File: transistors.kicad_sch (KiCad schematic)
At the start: 16 parts, among them J11 Transistor_2, J12 Transistor_1, J13 Transistor_4, J14 Transistor_.3, Q1 DMN2011UTS, Q2 DMN2011UTS, Q3 DMN2011UTS, Q4 DMN2011UTS

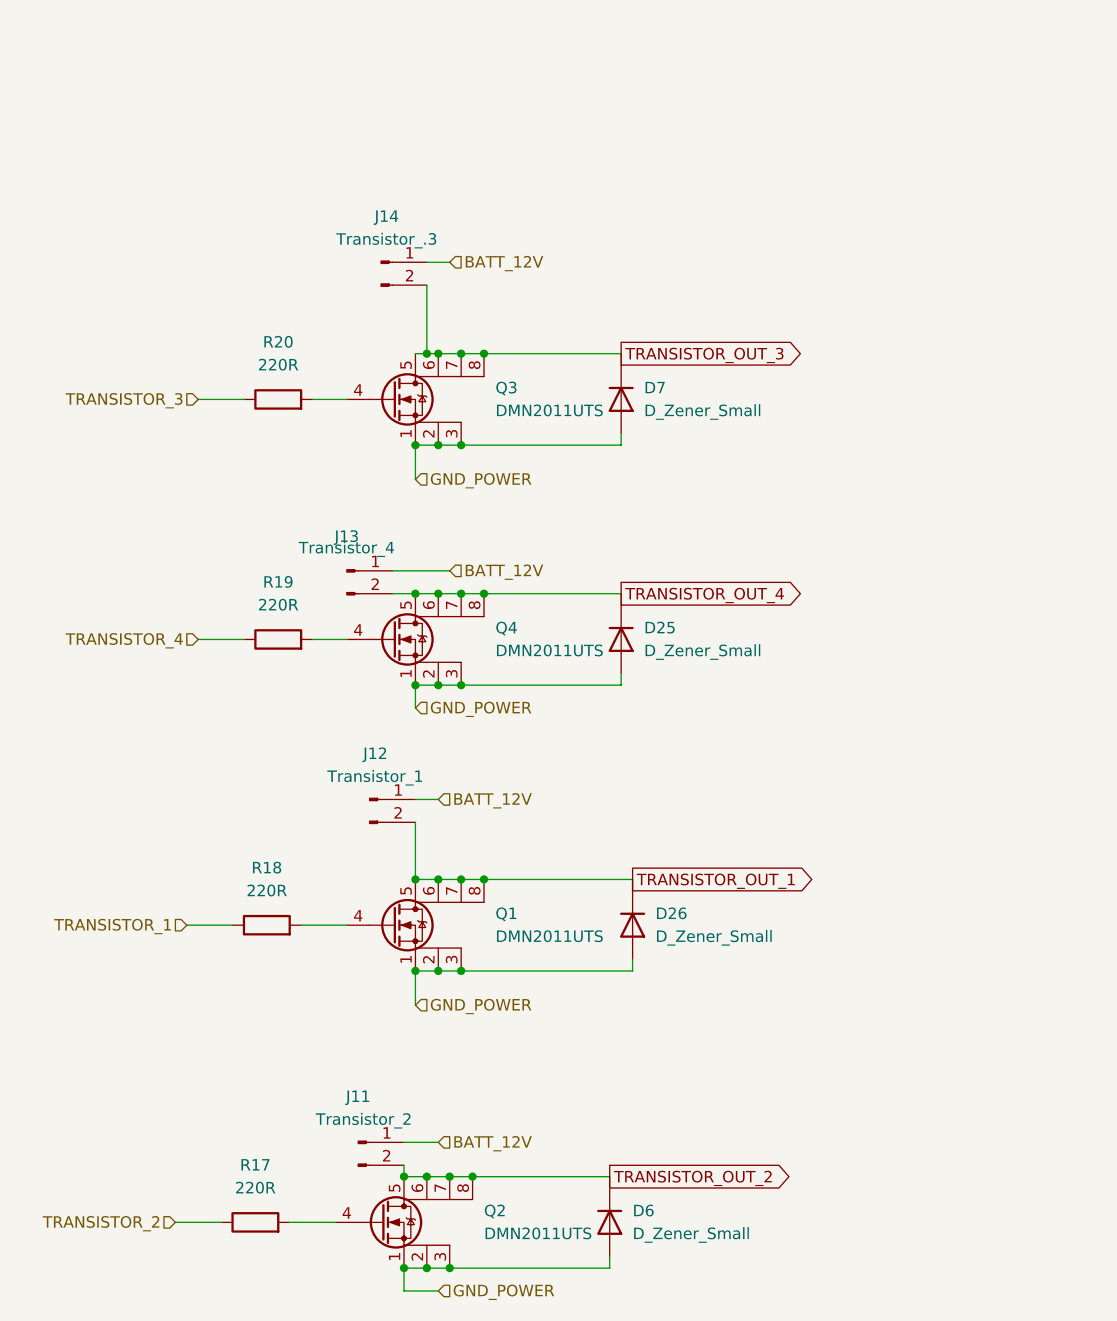
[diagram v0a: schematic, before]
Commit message: add possibility to have 2 of the transistor outputs to use either 12V or 24V
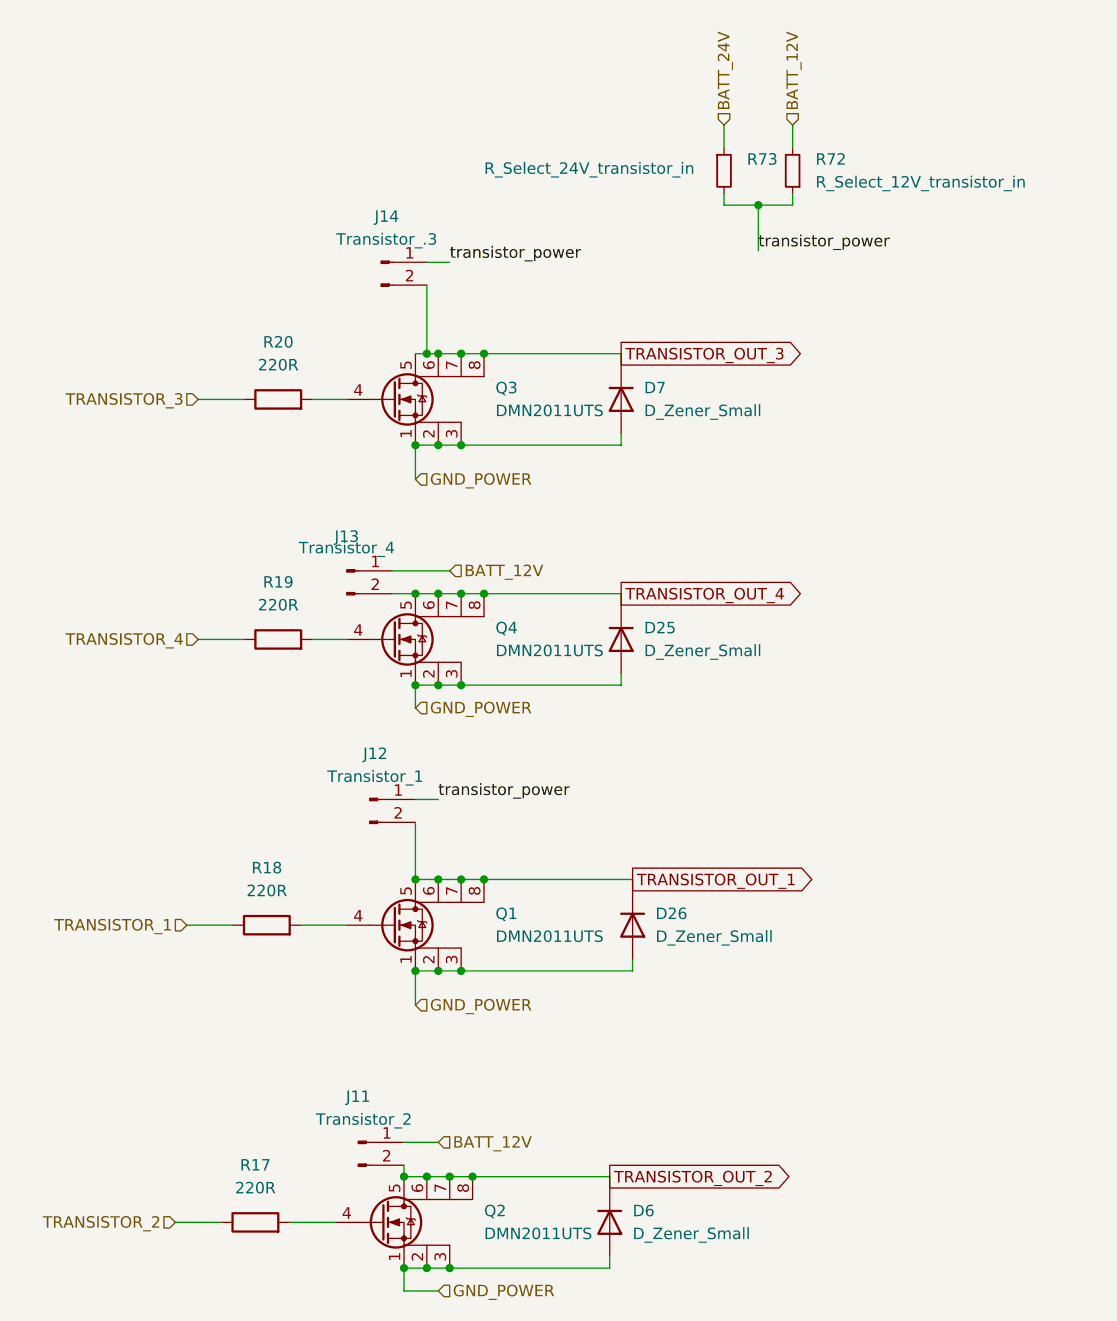
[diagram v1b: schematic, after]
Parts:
- added R72: R_Select_12V_transistor_in, Resistor_SMD:R_1206_3216Metric, symbol Device:R_Small
- added R73: R_Select_24V_transistor_in, Resistor_SMD:R_1206_3216Metric, symbol Device:R_Small
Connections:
- net BATT_12V: now also R72.2; no longer J12.1 (Pin_1), J14.1 (Pin_1)
- new net BATT_24V: R73.1
- new net transistor_power: J12.1 (Pin_1), J14.1 (Pin_1), R72.1, R73.2
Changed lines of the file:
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@@
+	)
+	(junction
+		(at 227.33 34.29)
+		(diameter 0)
+		(color 0 0 0 0)
 	)
 	(junction
@@
 	(wire
 		(pts
+			(xy 223.52 33.02) (xy 223.52 34.29)
+		)
+		(stroke
+			(width 0)
+			(type default)
+		)
+	)
+	(wire
+		(pts
 			(xy 189.23 87.63) (xy 191.77 87.63)
 		)
@@
 	(wire
 		(pts
+			(xy 231.14 34.29) (xy 231.14 33.02)
+		)
+		(stroke
+			(width 0)
+			(type default)
+		)
+	)
+	(wire
+		(pts
 			(xy 190.5 50.8) (xy 191.77 50.8)
 		)
@@
 	(wire
 		(pts
+			(xy 231.14 25.4) (xy 231.14 27.94)
+		)
+		(stroke
+			(width 0)
+			(type default)
+		)
+	)
+	(wire
+		(pts
 			(xy 189.23 60.96) (xy 191.77 60.96)
 		)
@@
 	(wire
 		(pts
+			(xy 223.52 34.29) (xy 227.33 34.29)
+		)
+		(stroke
+			(width 0)
+			(type default)
+		)
+	)
+	(wire
+		(pts
 			(xy 194.31 60.96) (xy 212.09 60.96)
 		)
@@
 	(wire
 		(pts
+			(xy 223.52 25.4) (xy 223.52 27.94)
+		)
+		(stroke
+			(width 0)
+			(type default)
+		)
+	)
+	(wire
+		(pts
 			(xy 189.23 60.96) (xy 189.23 64.77)
 		)
@@
 	(wire
 		(pts
+			(xy 231.14 34.29) (xy 227.33 34.29)
+		)
+		(stroke
+			(width 0)
+			(type default)
+		)
+	)
+	(wire
+		(pts
+			(xy 227.33 34.29) (xy 227.33 39.37)
+		)
+		(stroke
+			(width 0)
+			(type default)
+		)
+	)
+	(wire
+		(pts
 			(xy 187.96 154.94) (xy 187.96 152.4)
 		)
@@
 			(width 0)
 			(type default)
+		)
+	)
+	(label "transistor_power"
+		(at 191.77 100.33 0)
+		(effects
+			(font
+				(size 1.27 1.27)
+			)
+			(justify left bottom)
+		)
+	)
+	(label "transistor_power"
+		(at 193.04 40.64 0)
+		(effects
+			(font
+				(size 1.27 1.27)
+			)
+			(justify left bottom)
+		)
+	)
+	(label "transistor_power"
+		(at 227.33 39.37 0)
+		(effects
+			(font
+				(size 1.27 1.27)
+			)
+			(justify left bottom)
 		)
 	)
@@
 		)
 	)
-	(hierarchical_label "BATT_12V"
-		(shape input)
-		(at 193.04 40.64 0)
-		(effects
-			(font
-				(size 1.27 1.27)
-			)
-			(justify left)
-		)
-	)
 	(hierarchical_label "GND_POWER"
 		(shape input)
@@
 		)
 	)
+	(hierarchical_label "BATT_12V"
+		(shape input)
+		(at 193.04 74.93 0)
+		(effects
+			(font
+				(size 1.27 1.27)
+			)
+			(justify left)
+		)
+	)
 	(hierarchical_label "GND_POWER"
 		(shape input)
@@
 		)
 	)
-	(hierarchical_label "BATT_12V"
-		(shape input)
-		(at 191.77 100.33 0)
-		(effects
-			(font
-				(size 1.27 1.27)
-			)
-			(justify left)
-		)
-	)
 	(hierarchical_label "TRANSISTOR_1"
 		(shape input)
@@
 		)
 	)
+	(hierarchical_label "BATT_24V"
+		(shape input)
+		(at 223.52 25.4 90)
+		(effects
+			(font
+				(size 1.27 1.27)
+			)
+			(justify left)
+		)
+	)
 	(hierarchical_label "BATT_12V"
 		(shape input)
-		(at 193.04 74.93 0)
+		(at 231.14 25.4 90)
 		(effects
 			(font
@@
 	)
 	(symbol
+		(lib_id "Device:R_Small")
+		(at 223.52 30.48 0)
+		(unit 1)
+		(exclude_from_sim no)
+		(in_bom yes)
+		(on_board yes)
+		(dnp no)
+		(property "Reference" "R73"
+			(at 226.06 29.2099 0)
+			(effects
+				(font
+					(size 1.27 1.27)
+				)
+				(justify left)
+			)
+		)
+		(property "Value" "R_Select_24V_transistor_in"
+			(at 196.85 30.226 0)
+			(effects
+				(font
+					(size 1.27 1.27)
+				)
+				(justify left)
+			)
+		)
+		(property "Footprint" "Resistor_SMD:R_1206_3216Metric"
+			(at 223.52 30.48 0)
+			(effects
+				(font
+					(size 1.27 1.27)
+				)
+				(hide yes)
+			)
+		)
+		(property "Datasheet" "~"
+			(at 223.52 30.48 0)
+			(effects
+				(font
+					(size 1.27 1.27)
+				)
+				(hide yes)
+			)
+		)
+		(property "Description" "Resistor, small symbol"
+			(at 223.52 30.48 0)
+			(effects
+				(font
+					(size 1.27 1.27)
+				)
+				(hide yes)
+			)
+		)
+		(pin "2"
+		)
+		(pin "1"
+		)
+		(instances
+			(project "carte_servo"
+				(path "/e63e39d7-6ac0-4ffd-8aa3-1841a4541b55/8cf8b4bb-2251-4ebd-baba-4f57c988e66e"
+					(reference "R73")
+					(unit 1)
+				)
+			)
+		)
+	)
+	(symbol
 		(lib_id "Device:D")
 		(at 212.09 55.88 270)
@@
 					(unit 1)
 				)
+			)
+		)
+	)
+	(symbol
+		(lib_id "Device:R_Small")
+		(at 231.14 30.48 180)
+		(unit 1)
+		(exclude_from_sim no)
+		(in_bom yes)
+		(on_board yes)
+		(dnp no)
+		(fields_autoplaced yes)
+		(property "Reference" "R72"
+			(at 233.68 29.2099 0)
+			(effects
+				(font
+					(size 1.27 1.27)
+				)
+				(justify right)
+			)
+		)
+		(property "Value" "R_Select_12V_transistor_in"
+			(at 233.68 31.7499 0)
+			(effects
+				(font
+					(size 1.27 1.27)
+				)
+				(justify right)
+			)
+		)
+		(property "Footprint" "Resistor_SMD:R_1206_3216Metric"
+			(at 231.14 30.48 0)
+			(effects
+				(font
+					(size 1.27 1.27)
+				)
+				(hide yes)
+			)
+		)
+		(property "Datasheet" "~"
+			(at 231.14 30.48 0)
+			(effects
+				(font
+					(size 1.27 1.27)
+				)
+				(hide yes)
+			)
+		)
+		(property "Description" "Resistor, small symbol"
+			(at 231.14 30.48 0)
+			(effects
+				(font
+					(size 1.27 1.27)
+				)
+				(hide yes)
+			)
+		)
+		(pin "2"
+		)
+		(pin "1"
+		)
+		(instances
+			(project "carte_servo"
+				(path "/e63e39d7-6ac0-4ffd-8aa3-1841a4541b55/8cf8b4bb-2251-4ebd-baba-4f57c988e66e"
+					(reference "R72")
+					(unit 1)
+				)

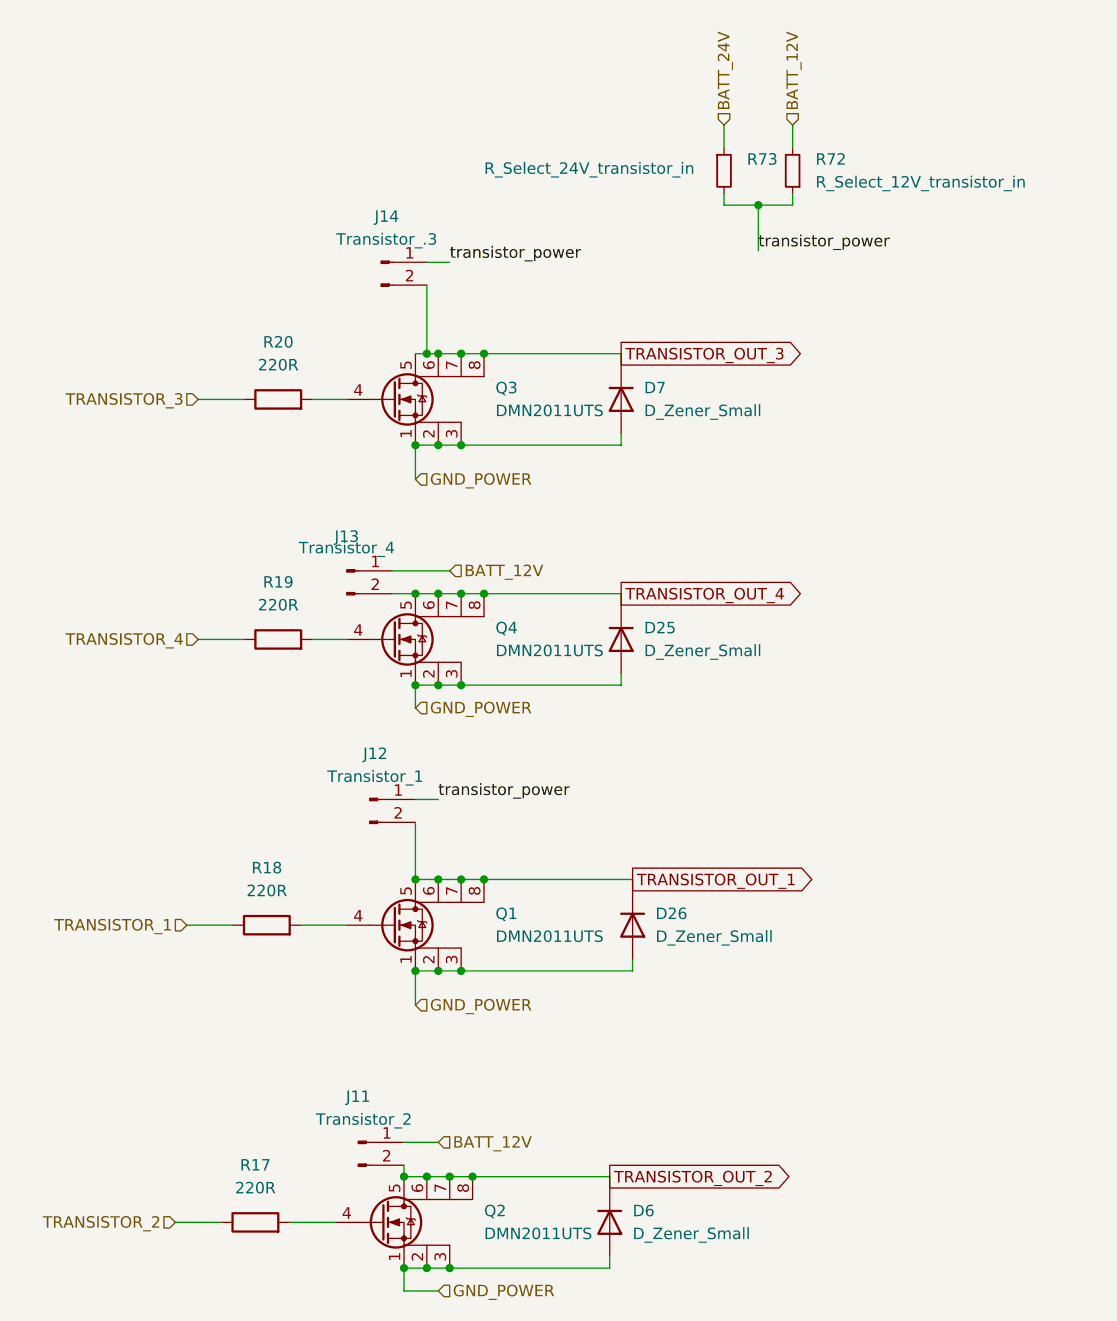
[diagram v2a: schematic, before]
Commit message: fix warnings + add big capa on 6V DCDC input
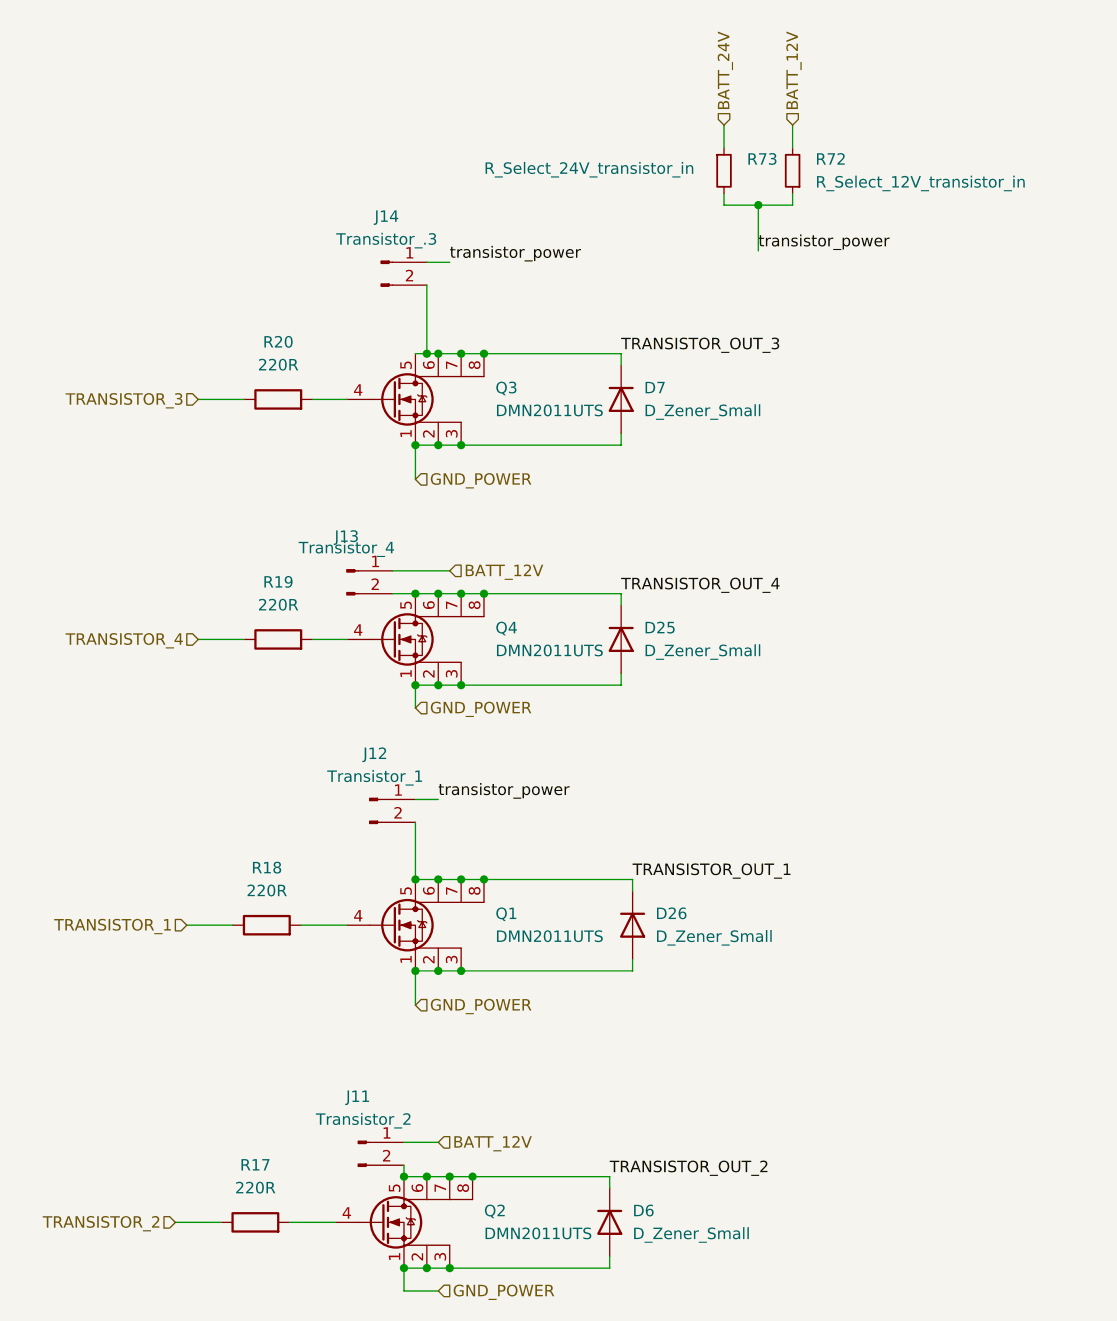
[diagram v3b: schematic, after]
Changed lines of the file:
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@@
+		)
+	)
+	(label "TRANSISTOR_OUT_3"
+		(at 212.09 50.8 0)
+		(effects
+			(font
+				(size 1.27 1.27)
+			)
+			(justify left bottom)
+		)
+	)
+	(label "TRANSISTOR_OUT_4"
+		(at 212.09 77.47 0)
+		(effects
+			(font
+				(size 1.27 1.27)
+			)
+			(justify left bottom)
 		)
 	)
@@
 		)
 	)
-	(global_label "TRANSISTOR_OUT_1"
-		(shape output)
-		(at 213.36 109.22 0)
-		(fields_autoplaced yes)
+	(label "TRANSISTOR_OUT_2"
+		(at 210.82 142.24 0)
 		(effects
 			(font
 				(size 1.27 1.27)
 			)
-			(justify left)
-		)
-		(property "Intersheetrefs" "${INTERSHEET_REFS}"
-			(at 233.795 109.1406 0)
-			(effects
-				(font
-					(size 1.27 1.27)
-				)
-				(justify left)
-				(hide yes)
-			)
+			(justify left bottom)
 		)
 	)
-	(global_label "TRANSISTOR_OUT_2"
-		(shape output)
-		(at 210.82 142.24 0)
-		(fields_autoplaced yes)
+	(label "TRANSISTOR_OUT_1"
+		(at 213.36 109.22 0)
 		(effects
 			(font
 				(size 1.27 1.27)
 			)
-			(justify left)
-		)
-		(property "Intersheetrefs" "${INTERSHEET_REFS}"
-			(at 231.255 142.1606 0)
-			(effects
-				(font
-					(size 1.27 1.27)
-				)
-				(justify left)
-				(hide yes)
-			)
+			(justify left bottom)
 		)
 	)
-	(global_label "TRANSISTOR_OUT_3"
-		(shape output)
-		(at 212.09 50.8 0)
-		(fields_autoplaced yes)
-		(effects
-			(font
-				(size 1.27 1.27)
-			)
-			(justify left)
-		)
-		(property "Intersheetrefs" "${INTERSHEET_REFS}"
-			(at 232.525 50.7206 0)
-			(effects
-				(font
-					(size 1.27 1.27)
-				)
-				(justify left)
-				(hide yes)
-			)
-		)
-	)
-	(global_label "TRANSISTOR_OUT_4"
-		(shape output)
-		(at 212.09 77.47 0)
-		(fields_autoplaced yes)
-		(effects
-			(font
-				(size 1.27 1.27)
-			)
-			(justify left)
-		)
-		(property "Intersheetrefs" "${INTERSHEET_REFS}"
-			(at 232.525 77.3906 0)
-			(effects
-				(font
-					(size 1.27 1.27)
-				)
-				(justify left)
-				(hide yes)
-			)
-		)
-	)
